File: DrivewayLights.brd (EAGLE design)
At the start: 69.8 x 83.8 mm, 36 parts, among them U1 TLC59108PW

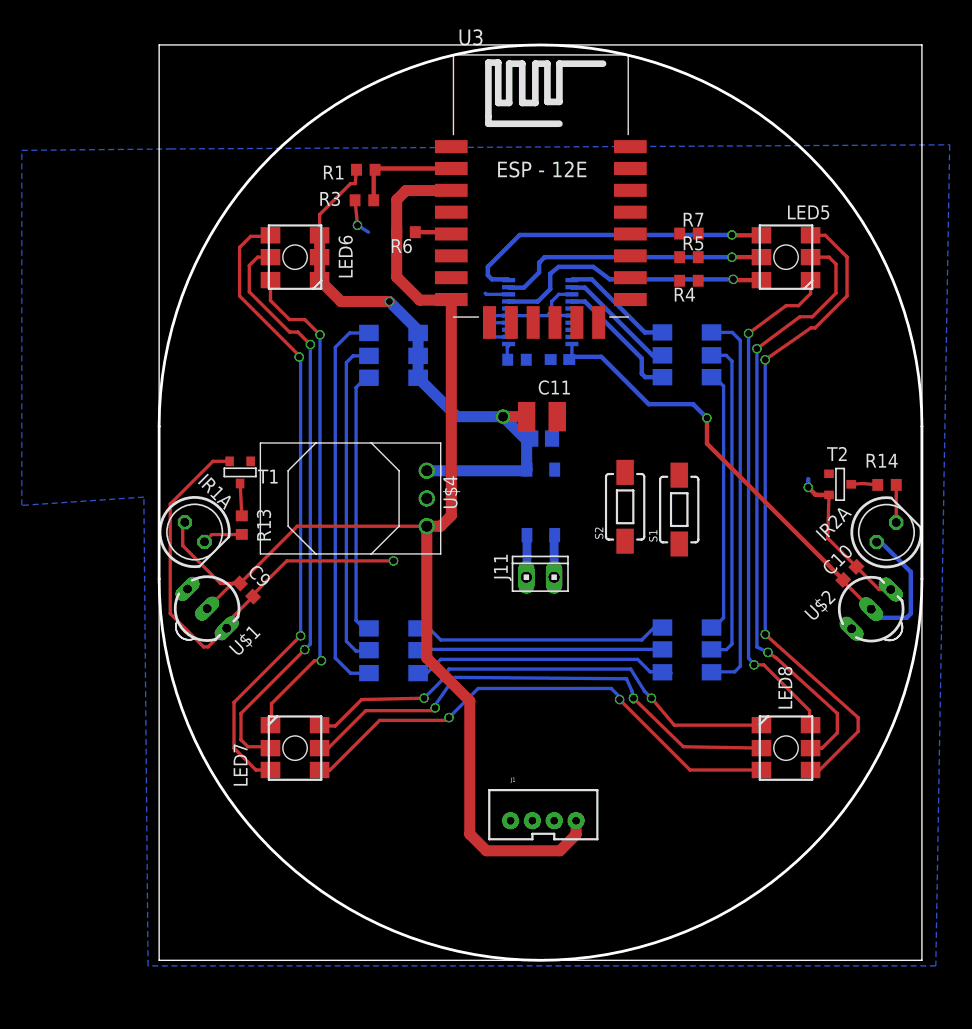
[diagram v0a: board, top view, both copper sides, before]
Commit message: Updates to board layout to bring dimensions back into where they should probably be.  Need to route board again, but hopefully this will now be good assuming the schematic is right.  Also capturing last rounds models and 3d print files
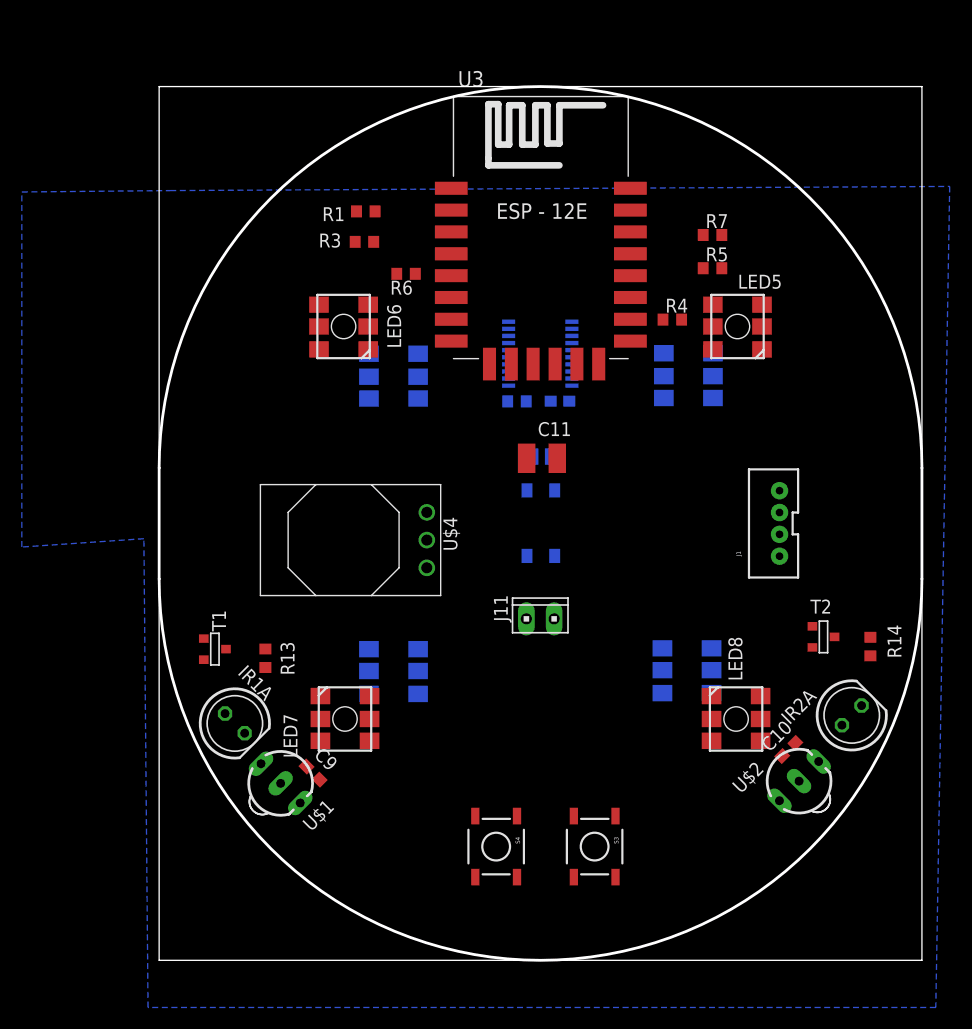
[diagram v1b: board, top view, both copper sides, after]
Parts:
- removed S1, S2: SWITCH-MOMENTARY-2SMD-1101NE, SparkFun-Electromechanical:TACTILE-SWITCH-1101NE
- added S3, S4: SWITCH-MOMENTARY-2SMD, SparkFun-Electromechanical:TACTILE-SWITCH-SMD
- moved J1 34.0 mm to (56.3, 40.0), turned to 90 degrees
- moved IR1A 17.9 mm to (6.93, 21.7)
- moved C9 17.8 mm to (14.1, 17.1)
- moved U$1 17.4 mm to (11.1, 16.2)
- moved U$2 17.1 mm to (58.6, 16.4)
- moved C10 17.1 mm to (57.7, 19.3)
- moved IR2A 17.1 mm to (63.4, 22.4)
- moved T1 16.4 mm to (5.11, 28.5), turned to 90 degrees
- moved R14 14.9 mm to (65.1, 28.7), turned to 270 degrees
- moved T2 14.1 mm to (60.8, 29.6)
- moved R13 12.4 mm to (9.73, 27.7)
- moved LED5 7.75 mm to (53.0, 58.0)
- moved LED6 7.75 mm to (16.9, 58.0)
- moved LED8 5.29 mm to (52.8, 22.1)
- moved LED7 5.29 mm to (17.0, 22.1)
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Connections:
- net FLASH_N: now also S3.1; no longer S1.1
- net GND: now also S3.3, S4.3; no longer S1.2, S2.2
- net RESET_N: now also S4.1; no longer S2.1
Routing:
- net 3.3V: track 167.1 -> 0.00 mm, vias 1 -> 0
- net GND: track 77.5 -> 0.00 mm, vias 3 -> 0
- net N$25: track 61.0 -> 0.00 mm, vias 2 -> 0
- net N$27: track 58.1 -> 0.00 mm, vias 2 -> 0
- net N$30: track 56.1 -> 0.00 mm, vias 2 -> 0
- net N$28: track 54.1 -> 0.00 mm, vias 2 -> 0
- net VCAP: track 53.8 -> 0.00 mm, vias 2 -> 0
- net N$29: track 47.4 -> 0.00 mm, vias 2 -> 0
- net N$31: track 46.9 -> 0.00 mm, vias 2 -> 0
- net N$26: track 46.8 -> 0.00 mm, vias 2 -> 0
- net N$33: track 45.8 -> 0.00 mm, vias 2 -> 0
- net N$32: track 45.5 -> 0.00 mm, vias 2 -> 0
- net N$21: track 35.7 -> 0.00 mm
- net N$18: track 35.6 -> 0.00 mm
- net N$15: track 30.3 -> 0.00 mm
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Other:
- board size 69.8 x 83.8 mm -> 69.8 x 80 mm

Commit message: Updates to schematic and relayout board
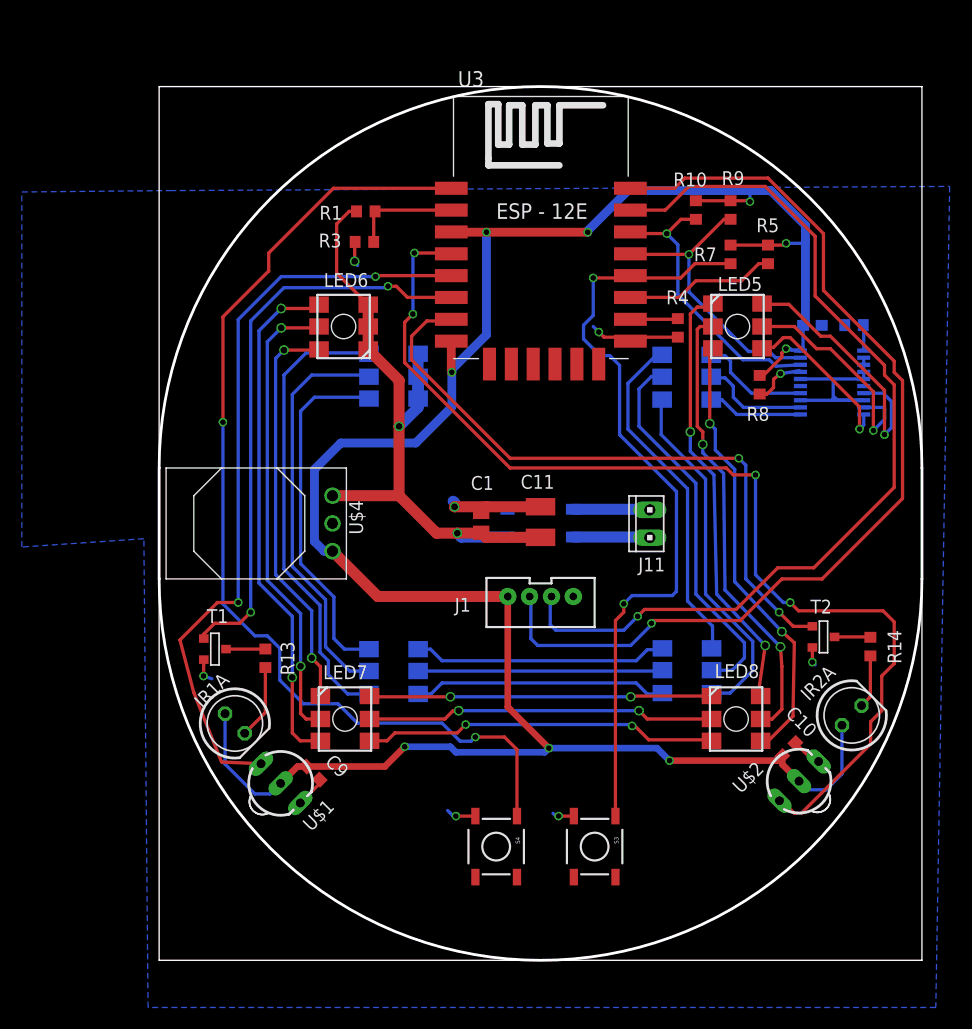
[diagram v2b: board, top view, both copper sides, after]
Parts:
- removed R6: 1k, resistor:R0603
- added R10, R9: 10k, resistor:R0603
- added R8: 1k, resistor:R0603
- moved R2 31.6 mm to (63.6, 58.2), turned to 180 degrees
- moved U1 26.9 mm to (61.6, 52.9), turned to 270 degrees
- moved C7 24.1 mm to (59.8, 58.1), turned to 180 degrees
- moved J1 22.5 mm to (34.9, 32.8), turned to 180 degrees
- moved J11 13.3 mm to (44.9, 40.0), turned to 90 degrees
- moved U$4 8.77 mm to (15.9, 40.0)
- moved C1 8.18 mm to (29.5, 40.1), flipped to the top, turned to 90 degrees
- moved C11 5.84 mm to (34.9, 40.1), turned to 90 degrees
- moved R5 5.24 mm to (55.8, 64.6), turned to 90 degrees
- moved R7 2.43 mm to (52.3, 64.6), turned to 90 degrees
- moved R4 0.92 mm to (47.5, 57.9), turned to 90 degrees
- moved LED9 0.16 mm to (48.3, 53.4), turned to 180 degrees
- moved B1 0.05 mm to (34.9, 40.0), turned to 90 degrees
- turned LED5 to 0 degrees
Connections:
- new net BLUE_LED: R5.1, U3.GPIO2
- net 3.3V: now also R10.2, R8.2, R9.2; no longer R6.2
- net IR_IN1: now also U3.GPIO14; no longer U3.GPIO4
- net IR_IN2: now also U3.GPIO16; no longer U3.GPIO5
- net LED_NRESET: now also R8.1; no longer U3.GPIO16
- net LED_SCL: now also R10.1, U3.GPIO5; no longer R6.1, U3.GPIO14
- net LED_SDA: now also R9.1, U3.GPIO4; no longer R5.1, U3.GPIO2
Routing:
- net 3.3V: track 0.00 -> 214.0 mm, vias 0 -> 9
- net IR_IN2: track 0.00 -> 97.4 mm, vias 0 -> 4
- net RESET_N: track 0.00 -> 93.6 mm, vias 0 -> 2
- net TX: track 0.00 -> 91.4 mm, vias 0 -> 1
- net RX: track 0.00 -> 85.5 mm, vias 0 -> 1
- net FLASH_N: track 0.00 -> 71.6 mm, vias 0 -> 2
- net IR_IN1: track 0.00 -> 69.3 mm, vias 0 -> 2
- net VCAP: track 0.00 -> 64.3 mm, vias 0 -> 2
- net IRLED2: track 0.00 -> 59.4 mm, vias 0 -> 2
- net GND: track 0.00 -> 52.9 mm, vias 0 -> 7
- net IRLED1: track 0.00 -> 52.3 mm, vias 0 -> 2
- net N$27: track 0.00 -> 47.5 mm, vias 0 -> 2
- net N$28: track 0.00 -> 42.6 mm, vias 0 -> 2
- net N$21: track 0.00 -> 42.2 mm
- net N$30: track 0.00 -> 41.7 mm, vias 0 -> 2
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
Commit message: Renamed parts and cleaned up silkscreen on board to prepare for next build
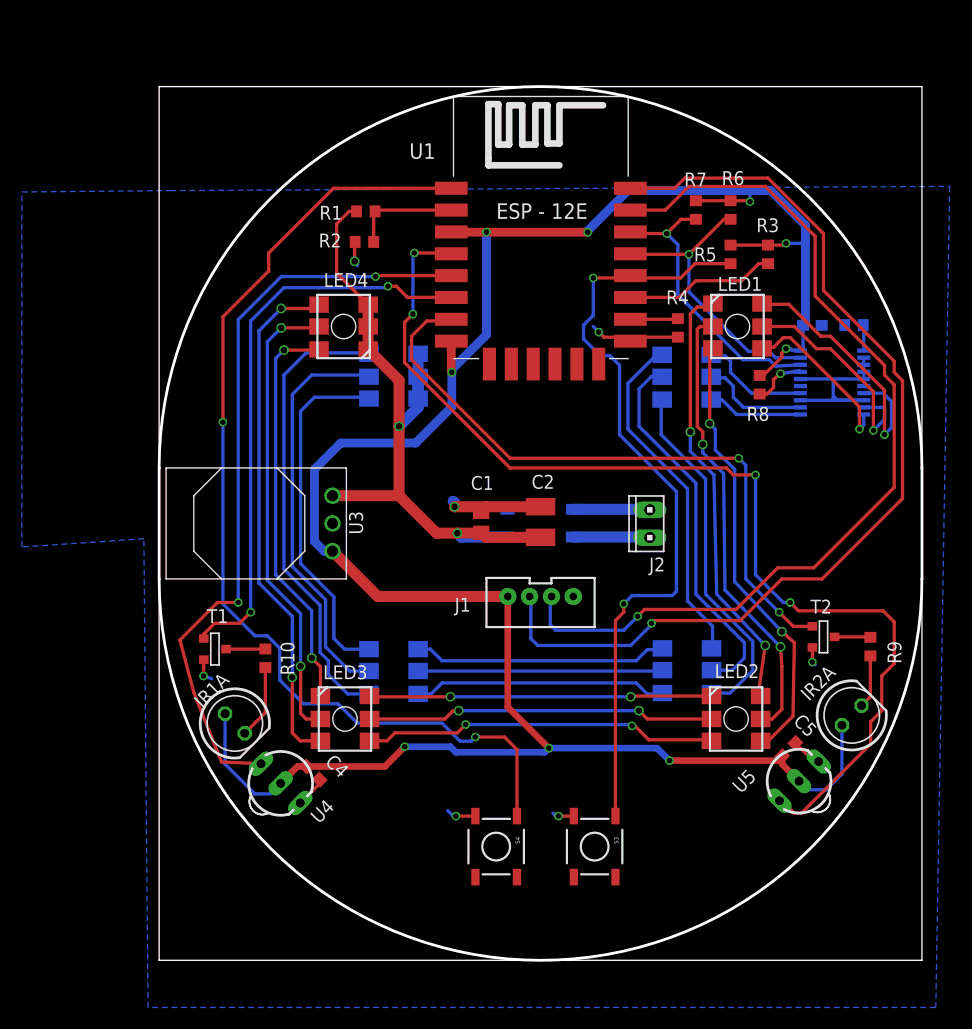
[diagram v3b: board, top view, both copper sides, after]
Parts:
- removed LED10, LED11, LED12, LED9: CLP6C, led:CLP6C
- removed R13, R14: 10, rcl:R0603
- removed U$4: DCDC_OKI-78SR, rwt-library:OKI-78SRH
- added LED1, LED2, LED3, LED4: CLP6C, led:CLP6C
- added R11: 625, rcl:R0603
- added R6: 10k, resistor:R0603
- added U2: TLC59108PW, texas:PW_R-PDSO-G20
- R10, R9: value 10k -> 10; device resistor:R0603 -> rcl:R0603
- R2: value 625 -> 1k; device rcl:R0603 -> resistor:R0603
- R7: value 1k -> 10k
- U1: value TLC59108PW -> (none); device texas:PW_R-PDSO-G20 -> esp8266modules:ESP12E-SMD
- U3: value (none) -> DCDC_OKI-78SR; device esp8266modules:ESP12E-SMD -> rwt-library:OKI-78SRH
- moved R10 56.9 mm to (9.73, 27.7), turned to 270 degrees
- moved R2 45.5 mm to (18.8, 65.8), flipped to the top, turned to 0 degrees
- moved LED6 44.5 mm to (48.3, 26.6), flipped to the bottom
- moved LED8 44.3 mm to (21.5, 53.4), flipped to the bottom
- moved R9 42.0 mm to (65.1, 28.7), turned to 270 degrees
- moved R3 37.0 mm to (55.8, 64.6), turned to 90 degrees
- moved U3 31.4 mm to (15.9, 40.0), turned to 90 degrees
- moved U1 29.1 mm to (35.1, 64.9), flipped to the top, turned to 0 degrees
- moved LED5 6.54 mm to (48.3, 53.4), flipped to the bottom, turned to 180 degrees
- moved LED7 6.25 mm to (21.5, 26.5), flipped to the bottom, turned to 180 degrees
- moved R7 5.16 mm to (49.1, 68.7)
- moved R5 3.43 mm to (52.3, 64.6)
- renumbered C10 to C5, C11 to C2, C7 to C3, C9 to C4, J11 to J2, U$1 to U4, U$2 to U5
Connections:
- net 3.3V: now also R3.2, R6.2, U1.CH_PD, U1.VCC, U2.20, U3.3; no longer R10.2, R9.2, U$4.3, U1.20, U3.CH_PD, U3.VCC
- net ADC: now also R2.2, U1.ADC; no longer R3.2, U3.ADC
- net BLUE: now also LED1.4, U2.10; no longer LED5.4, U1.10
- net BLUE2: now also LED5.4, U2.14; no longer LED9.4, U1.14
- net BLUE_LED: now also R3.1, U1.GPIO2; no longer R5.1, U3.GPIO2
- net FLASH_N: now also R5.1, U1.GPIO0; no longer R7.1, U3.GPIO0
- net GND: now also R11.1, U1.GND, U2.13, U2.16, U2.2, U2.3, U2.4, U2.5, U2.8, U3.2; no longer R3.1, U$4.2, U1.13, U1.16, U1.2, U1.3, U1.4, U1.5, U1.8, U3.GND
- net GREEN: now also LED1.5, U2.9; no longer LED5.5, U1.9
- net GREEN2: now also LED5.5, U2.12; no longer LED9.5, U1.12
- net IRLED0: now also U1.GPIO15; no longer U3.GPIO15
- net IRLED1: now also U1.GPIO12; no longer U3.GPIO12
- net IRLED2: now also U1.GPIO13; no longer U3.GPIO13
- net IR_IN1: now also U1.GPIO14; no longer U3.GPIO14
- net IR_IN2: now also U1.GPIO16; no longer U3.GPIO16
- net LED_CURRENT_R: now also R11.2, U2.1; no longer R2.2, U1.1
- net LED_NRESET: now also U2.17; no longer U1.17
- net LED_SCL: now also R7.1, U1.GPIO5, U2.18; no longer R10.1, U1.18, U3.GPIO5
- net LED_SDA: now also R6.1, U1.GPIO4, U2.19; no longer R9.1, U1.19, U3.GPIO4
- net N$12: now also LED5.3, LED6.4; no longer LED12.4, LED9.3
- net N$13: now also LED6.3, LED7.4; no longer LED11.4, LED12.3
- net N$14: now also LED7.3, LED8.4; no longer LED10.4, LED11.3
- net N$15: now also LED7.2, LED8.5; no longer LED10.5, LED11.2
- net N$16: now also LED6.2, LED7.5; no longer LED11.5, LED12.2
- net N$17: now also LED5.2, LED6.5; no longer LED12.5, LED9.2
- net N$18: now also LED5.1, LED6.6; no longer LED12.6, LED9.1
- net N$2: now also R9.2; no longer R14.2
- net N$20: now also LED6.1, LED7.6; no longer LED11.6, LED12.1
- net N$21: now also LED7.1, LED8.6; no longer LED10.6, LED11.1
- net N$25: now also LED1.3, LED2.4; no longer LED5.3, LED8.4
- net N$26: now also LED2.3, LED3.4; no longer LED7.4, LED8.3
- net N$27: now also LED3.3, LED4.4; no longer LED6.4, LED7.3
- net N$28: now also LED3.2, LED4.5; no longer LED6.5, LED7.2
- net N$29: now also LED2.2, LED3.5; no longer LED7.5, LED8.2
- net N$30: now also LED1.2, LED2.5; no longer LED5.2, LED8.5
- net N$31: now also LED1.1, LED2.6; no longer LED5.1, LED8.6
- net N$32: now also LED2.1, LED3.6; no longer LED7.6, LED8.1
- net N$33: now also LED3.1, LED4.6; no longer LED6.6, LED7.1
- net N$5: now also R10.2; no longer R13.2
- net N$6: now also R10.1; no longer R13.1
- net N$9: now also R9.1; no longer R14.1
- net RED: now also LED1.6, U2.7; no longer LED5.6, U1.7
- net RED2: now also LED5.6, U2.11; no longer LED9.6, U1.11
- net RESET_N: now also U1.RESET; no longer U3.RESET
- net RX: now also U1.RXD0; no longer U3.RXD0
- net TX: now also U1.TXD0; no longer U3.TXD0
- net VCAP: now also LED4.1, LED4.2, LED4.3, LED8.1, LED8.2, LED8.3, U3.1; no longer LED10.1, LED10.2, LED10.3, LED6.1, LED6.2, LED6.3, U$4.1
